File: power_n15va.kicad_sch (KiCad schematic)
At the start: 29 parts, among them U10 LT3579, U11 LT3093

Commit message: edit README.md
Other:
- company: (none) -> NOIRLab
- title: (none) -> 4 channel ADC Module
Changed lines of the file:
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@@
 	(generator_version "9.0")
 	(paper "A4")
+	(title_block
+		(title "4 channel ADC Module")
+		(date "2025-04-18")
+		(rev "0.1")
+		(company "NOIRLab")
+		(comment 1 "Design: Braulio Cancino Vera - braulio.cancino@noirlab.edu")
+	)
 	(text "OUTS and SET GND kelvin \nconnected to output capacitor\nto improve PSRR"
 		(exclude_from_sim no)

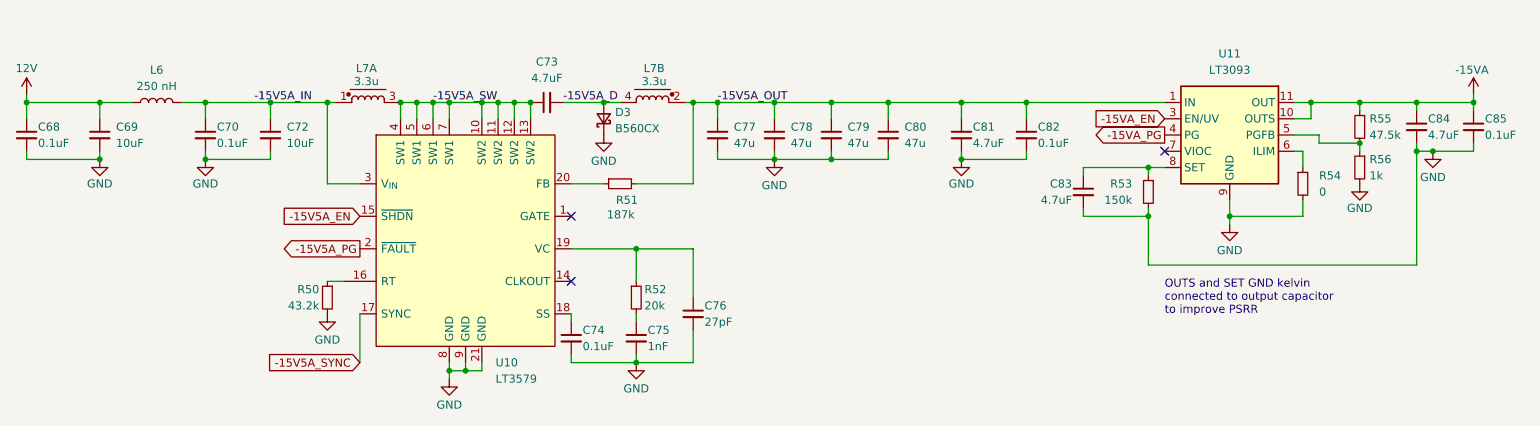
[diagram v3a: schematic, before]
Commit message: Split DC DC schematic and improve layout
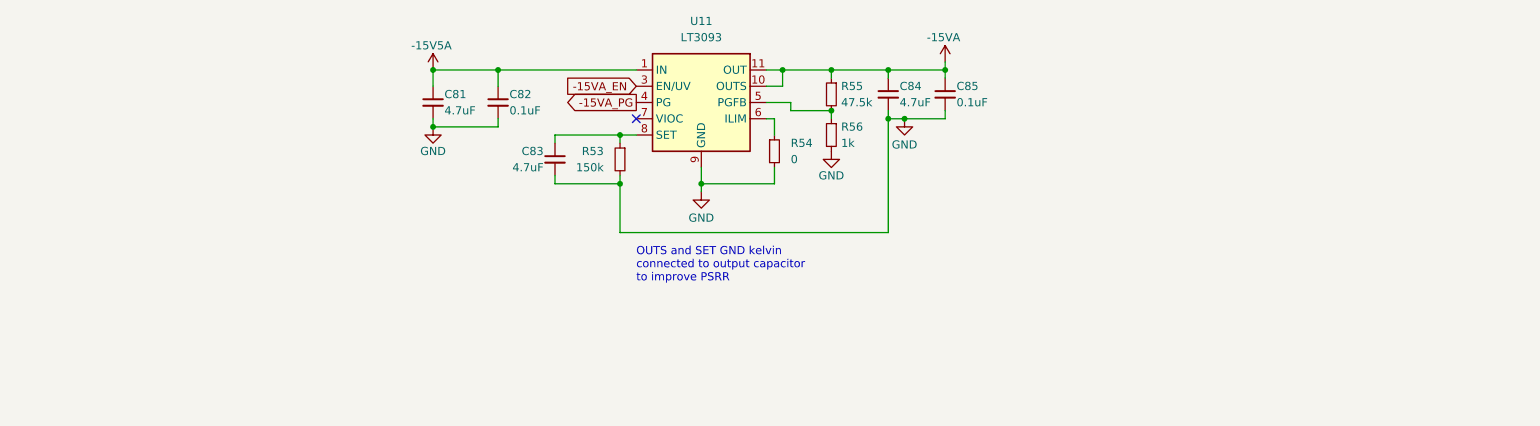
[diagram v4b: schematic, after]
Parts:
- removed C68, C70, C74: 0.1uF, Capacitor_SMD:C_0402_1005Metric, symbol Device:C_Small
- removed C69, C72: 10uF, Capacitor_SMD:C_1206_3216Metric, symbol Device:C_Small
- removed C73: 4.7uF, Capacitor_SMD:C_1210_3225Metric, symbol Device:C_Small
- removed C75: 1nF, Capacitor_SMD:C_0603_1608Metric, symbol Device:C_Small
- removed C76: 27pF, Capacitor_SMD:C_0603_1608Metric, symbol Device:C_Small
- removed C77, C78, C79, C80: 47u, Capacitor_SMD:C_1210_3225Metric, symbol Device:C_Small
- removed D3: B560CX, Diode_SMD:D_SMC, symbol Device:D_Schottky_Small
- removed L6: 250 nH, Inductor_SMD:L_1210_3225Metric, symbol Device:L
- removed L7: 3.3u, lib:DRQ125, symbol lib:DRQ
- removed R50: 43.2k, Resistor_SMD:R_0603_1608Metric, symbol Device:R_Small
- removed R51: 187k, Resistor_SMD:R_0603_1608Metric, symbol Device:R_Small
- removed R52: 20k, Resistor_SMD:R_0603_1608Metric, symbol Device:R_Small
- removed U10: LT3579, lib:LT3579-QFN, symbol lib:LT3579_QFN
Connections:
- net -15V5A_OUT renamed -15V5A
- no-connect marks 3 -> 1
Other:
- moved on the sheet: C81, C82, C83, C84, C85, R53, R54, R55, R56, U11
